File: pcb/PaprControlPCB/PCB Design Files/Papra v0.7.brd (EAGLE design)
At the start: 36 x 45 mm, 48 parts, among them Q1 BSS123, Q2 BSS123, U1 LP2985-50DBVR (C74511), U2 ATTINYX04SOIC14, U9 TPS259472ARPWR

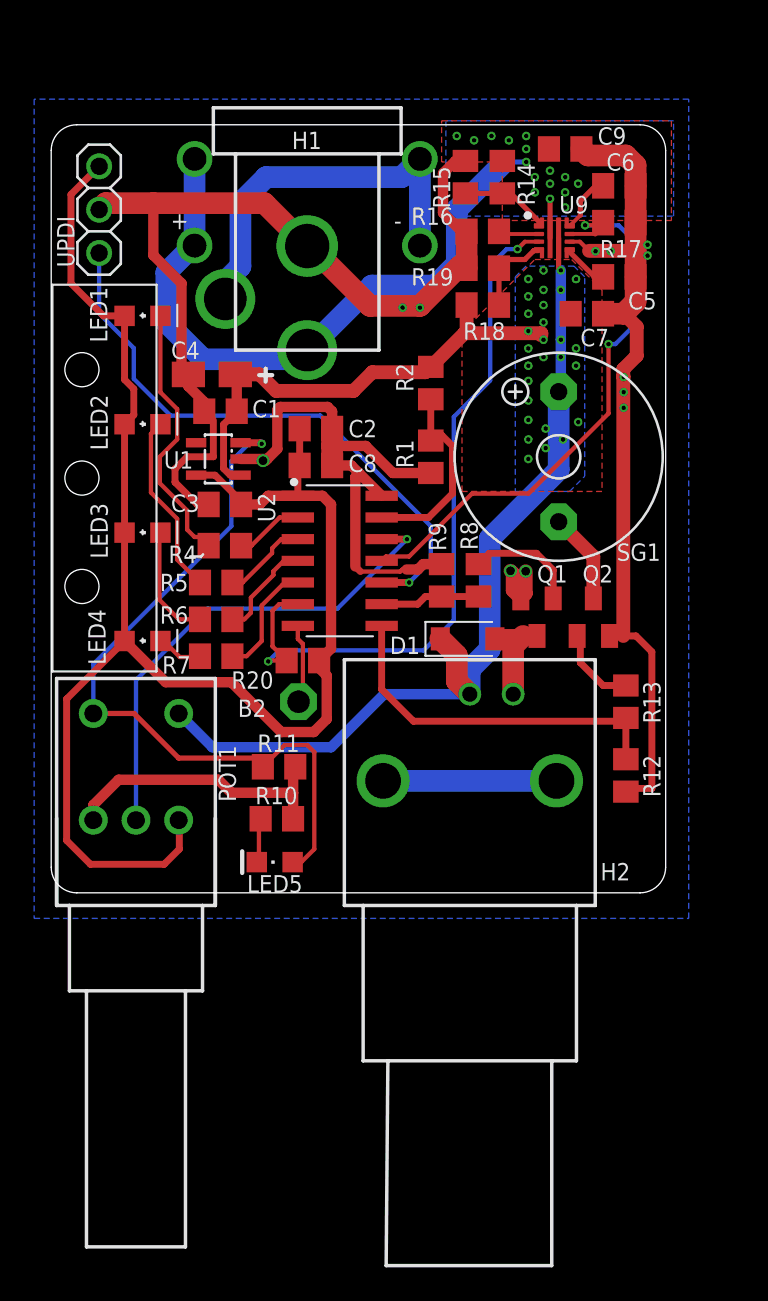
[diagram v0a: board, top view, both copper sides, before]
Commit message: Updating to v0.7
Closes #59
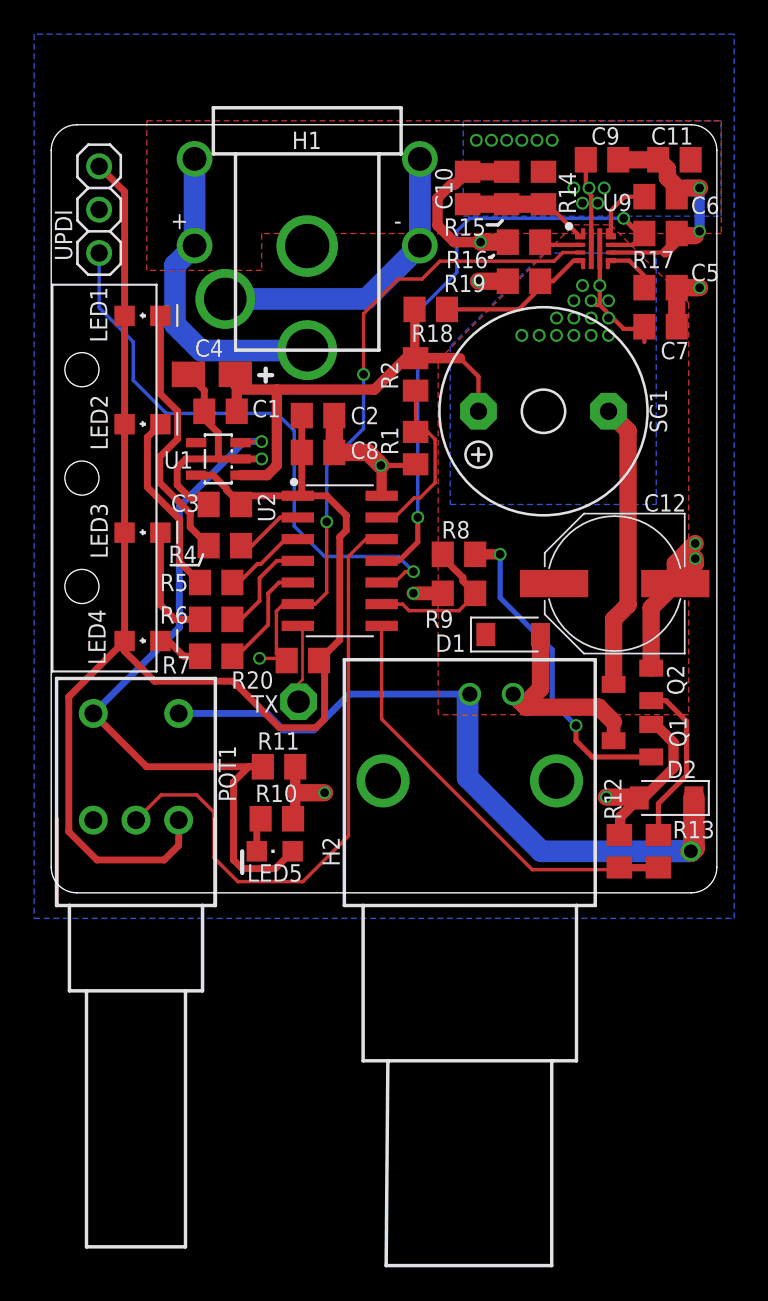
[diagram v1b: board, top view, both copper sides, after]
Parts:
- added +12V: PTR1B1,27, testpad:B1,27
- added C10: .1uF CL21B104KBFNNNE (C49678 ), rcl:C0805
- added C11: 1uF CL21B105KBFNNNE (C28323), rcl:C0805
- added C12: 220uF, rcl:PANASONIC_F
- added D2: MBR2H100SFT3G C96515, Diode:SODFL3718X115
- C7: value 1uF CL21B105KBFNNNE (C28323) -> 10uF
- moved Q1 9.14 mm to (19.1, -13.6), turned to 90 degrees
- moved R13 8.97 mm to (20.6, -20.1)
- moved Q2 4.55 mm to (19.1, -10.3), turned to 90 degrees
- moved R12 4.46 mm to (18.3, -20.1), turned to 270 degrees
- moved C7 4.38 mm to (20.7, 10.7)
- moved R18 3.06 mm to (7.24, 11.7)
- moved SG1 2.81 mm to (13.8, 5.71), turned to 180 degrees
- moved D1 2.68 mm to (12.1, -7.37)
- moved R19 2.53 mm to (12.7, 13.3)
- moved R14 2.50 mm to (13.8, 18.8)
- moved C5 2.50 mm to (20.7, 13.0)
- moved C6 2.50 mm to (20.7, 18.3)
- moved R17 2.50 mm to (20.7, 16.1)
- moved R15 2.50 mm to (11.7, 18.8)
- moved R16 2.50 mm to (12.7, 15.6)
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- renumbered B2 to TX
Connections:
- removed net PINS: H2.P$1, H2.P$2
- net +12V: now also +12V.TP, C12.+, D2.1
- net 12V-IN: now also C11.1
- net EN/UVLO: now also C10.1
- net GND: now also C10.2, C11.2, C12.-, D2.2
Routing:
- net GND: track 158.2 -> 82.0 mm
- net 12V-IN: track 41.5 -> 23.9 mm, vias 16 -> 11
- net FETGATE: track 6.71 -> 19.0 mm, vias 0 -> 2
- net BUZZER-GND: track 5.33 -> 16.8 mm
- net PINS: track 10.2 -> 0.00 mm
- net POT-ADC: track 29.0 -> 36.6 mm, vias 1 -> 0
- net FAN-GND: track 6.19 -> 13.1 mm
- net BUZZER: track 21.3 -> 27.7 mm
- net FETGATE1: track 4.87 -> 9.93 mm
- net GND-SWITCH: track 22.7 -> 17.8 mm
- net PGTH: track 4.95 -> 9.22 mm
- net PG: track 43.0 -> 39.3 mm, vias 2 -> 3
- net FAN-PWM: track 5.86 -> 9.17 mm
- net EN/UVLO: track 5.25 -> 7.38 mm
- net +5V: track 93.9 -> 92.1 mm
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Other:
- board size 36 x 45 mm -> 39 x 45 mm
- board text added: "05JAN2022"
- board text added: "PAPRA V0.7"
- board text removed: "27JULY2021"
- board text removed: "PAPRA V0.6"
